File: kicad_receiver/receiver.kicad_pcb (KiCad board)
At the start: 2 copper layers, 60 x 50 mm, 51 parts, among them J1 Conn_01x05_Male, J2 M1+, J3 M1-, J4 M2+, J5 M2-, J6 CHG+5V, J7 CHG-, J8 BAT+, J9 BAT-, U1 LP2985-3.3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

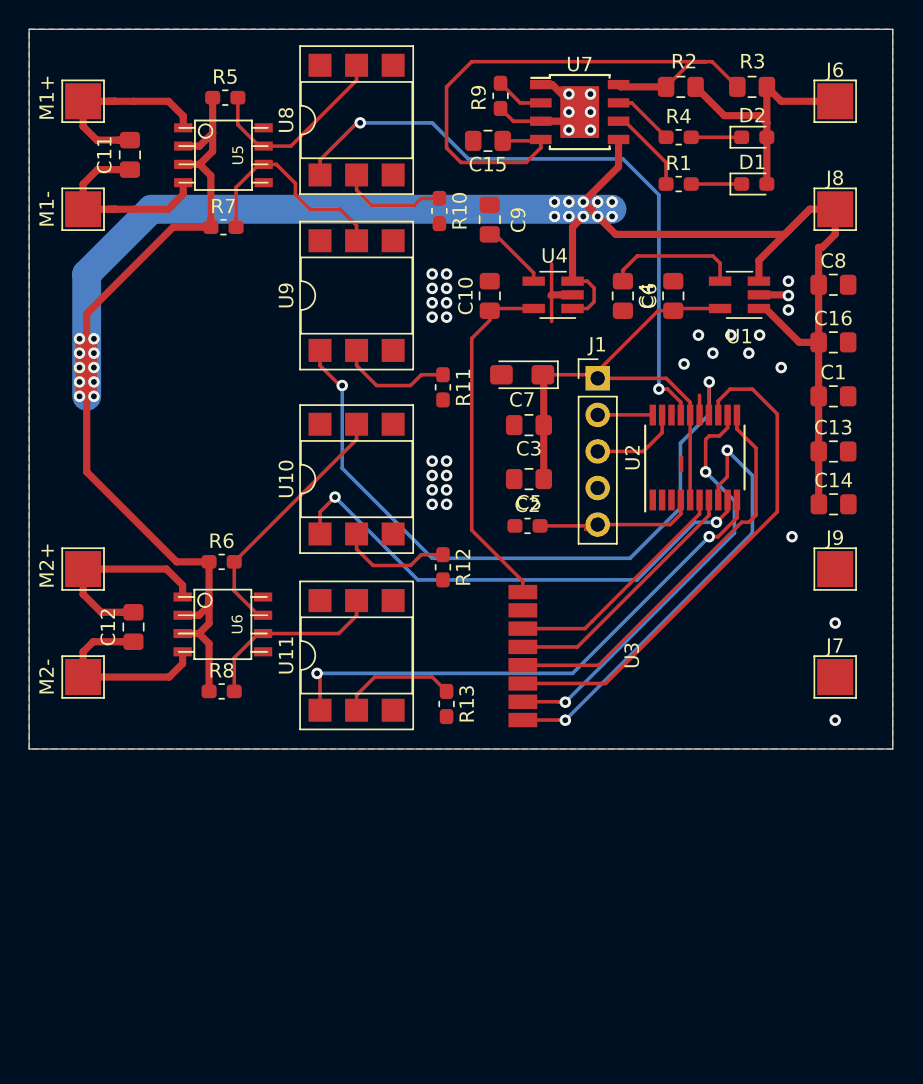
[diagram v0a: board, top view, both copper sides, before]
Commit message: optocouples removed
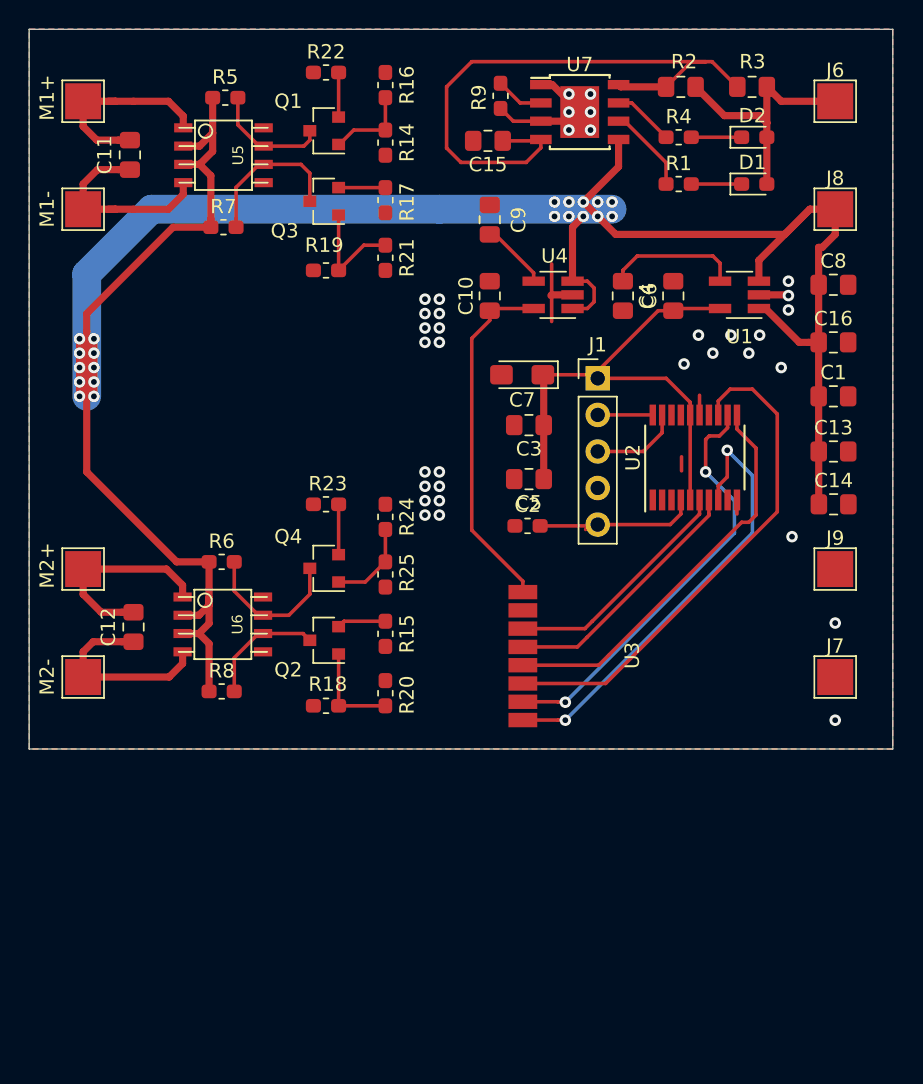
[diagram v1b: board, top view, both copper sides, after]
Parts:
- removed R10, R11, R12, R13: 220, Resistor_SMD:R_0603_1608Metric_Pad1.05x0.95mm_HandSolder
- removed U10, U11, U8, U9: 4N26, Package_DIP:DIP-6_W7.62mm_SMDSocket_SmallPads
- added Q1: MMBT3904, Package_TO_SOT_SMD:SOT-23, F.Cu at (147.5, 82.0)
- added Q2: MMBT3904, Package_TO_SOT_SMD:SOT-23, F.Cu at (147.5, 117.5)
- added Q3: MMBT3904, Package_TO_SOT_SMD:SOT-23, F.Cu at (147.5, 87.0)
- added Q4: MMBT3904, Package_TO_SOT_SMD:SOT-23, F.Cu at (147.5, 112.5)
- added R14: 1k, Resistor_SMD:R_0603_1608Metric_Pad1.05x0.95mm_HandSolder, F.Cu at (151.8, 82.9)
- added R15: 100, Resistor_SMD:R_0603_1608Metric_Pad1.05x0.95mm_HandSolder, F.Cu at (151.8, 117.0)
- added R16: 10k, Resistor_SMD:R_0603_1608Metric_Pad1.05x0.95mm_HandSolder, F.Cu at (151.8, 78.9)
- added R17: 100, Resistor_SMD:R_0603_1608Metric_Pad1.05x0.95mm_HandSolder, F.Cu at (151.8, 86.9)
- added R18: 10k, Resistor_SMD:R_0603_1608Metric_Pad1.05x0.95mm_HandSolder, F.Cu at (147.6, 122.0)
- added R19: 10k, Resistor_SMD:R_0603_1608Metric_Pad1.05x0.95mm_HandSolder, F.Cu at (147.6, 91.8)
- added R20: 1k, Resistor_SMD:R_0603_1608Metric_Pad1.05x0.95mm_HandSolder, F.Cu at (151.8, 121.1)
- added R21: 1k, Resistor_SMD:R_0603_1608Metric_Pad1.05x0.95mm_HandSolder, F.Cu at (151.8, 90.9)
- added R22: 100, Resistor_SMD:R_0603_1608Metric_Pad1.05x0.95mm_HandSolder, F.Cu at (147.6, 78.0)
- added R23: 100, Resistor_SMD:R_0603_1608Metric_Pad1.05x0.95mm_HandSolder, F.Cu at (147.6, 108.0)
- added R24: 10k, Resistor_SMD:R_0603_1608Metric_Pad1.05x0.95mm_HandSolder, F.Cu at (151.8, 108.9)
- added R25: 1k, Resistor_SMD:R_0603_1608Metric_Pad1.05x0.95mm_HandSolder, F.Cu at (151.8, 112.9)
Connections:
- U2 pad 18: Net-(U2-Pad18) -> (no net)
- U2 pad 2: Net-(U2-Pad2) -> (no net)
- U2 pad 3: Net-(U2-Pad3) -> (no net)
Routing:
- net FB_PWM: track 48.3 -> 0.00 mm, vias 2 -> 0
- net FF_PWM: track 44.0 -> 0.00 mm, vias 2 -> 0
- net TURN_RIGHT: track 39.0 -> 1.47 mm, vias 2 -> 0
- net TURN_LEFT: track 35.4 -> 0.00 mm, vias 2 -> 0
- net Net-(R13-Pad1): track 8.24 -> 0.00 mm
- net Net-(R11-Pad1): track 7.94 -> 0.00 mm
- net Net-(R12-Pad1): track 7.83 -> 0.00 mm
- net Net-(Q3-Pad1): track 0.00 -> 7.82 mm
- net Net-(R10-Pad1): track 7.45 -> 0.00 mm
- net Net-(Q4-Pad3): track 17.8 -> 10.4 mm
- net Net-(Q2-Pad1): track 0.00 -> 6.85 mm
- net Net-(Q4-Pad1): track 0.00 -> 6.08 mm
- net Net-(Q1-Pad1): track 0.00 -> 5.91 mm
- net Net-(Q1-Pad3): track 13.7 -> 8.32 mm
- net Net-(Q2-Pad3): track 13.1 -> 8.48 mm
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
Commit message: new route done
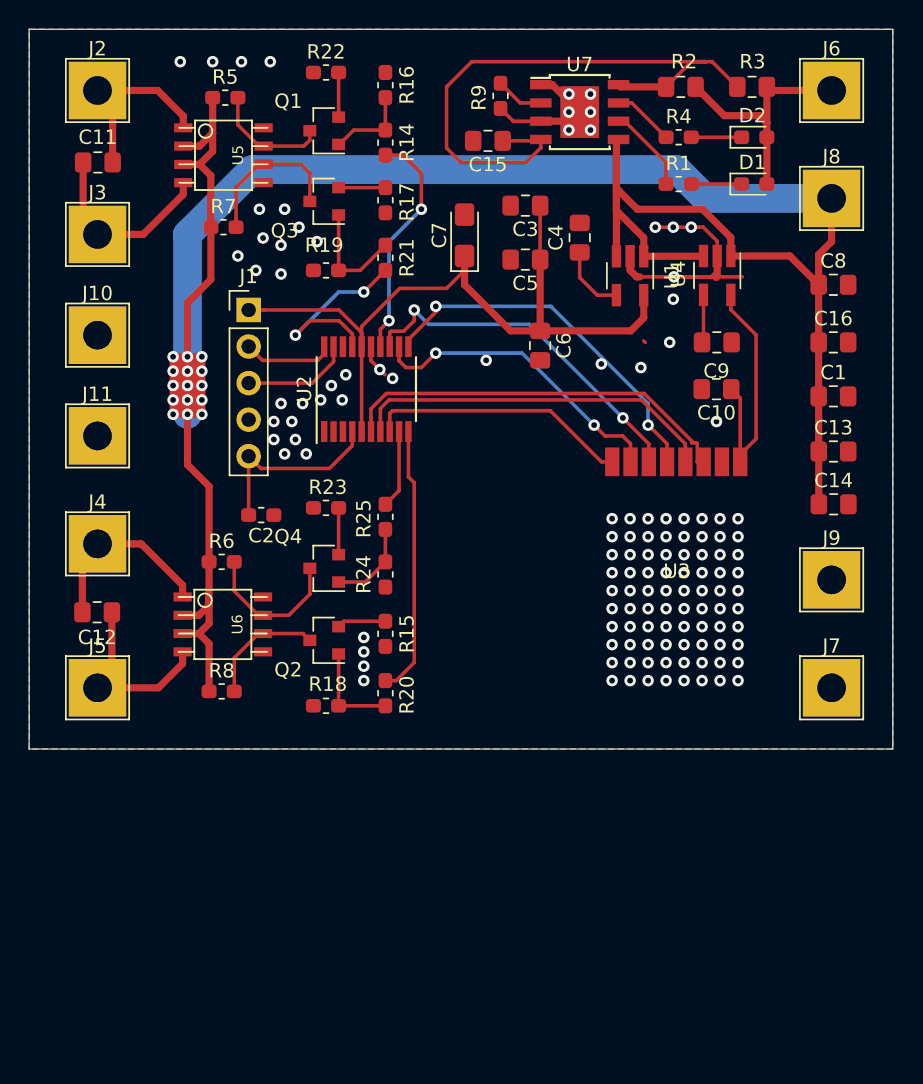
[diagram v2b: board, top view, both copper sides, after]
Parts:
- added J10: LIGHTS, TestPoint:TestPoint_THTPad_4.0x4.0mm_Drill2.0mm, F.Cu at (131.8, 96.2)
- added J11: BEEP, TestPoint:TestPoint_THTPad_4.0x4.0mm_Drill2.0mm, F.Cu at (131.8, 103.2)
- J2, J3, J4, J5, J6, J7, J8, J9: footprint TestPoint:TestPoint_Pad_2.5x2.5mm -> TestPoint:TestPoint_THTPad_4.0x4.0mm_Drill2.0mm
- moved J1 24.7 mm to (142.2, 94.5)
- moved U2 23.3 mm to (150.4, 100.0)
- moved C2 18.5 mm to (143.1, 108.8), turned to 180 degrees
- moved C9 17.9 mm to (174.8, 96.8), turned to 0 degrees
- moved C10 17.0 mm to (174.8, 100.0), turned to 180 degrees
- moved C3 15.3 mm to (161.5, 87.2)
- moved C5 15.3 mm to (161.5, 91.0)
- moved U4 11.5 mm to (174.8, 92.1), turned to 270 degrees
- moved C7 10.5 mm to (157.2, 89.3), turned to 90 degrees
- moved C6 9.87 mm to (162.5, 97.0), turned to 270 degrees
- moved U1 7.72 mm to (168.8, 92.1), turned to 270 degrees
- moved U3 5.15 mm to (172.0, 113.8), turned to 180 degrees
- moved C4 5.04 mm to (165.2, 89.5), turned to 90 degrees
- moved R24 4.00 mm to (151.8, 112.9), turned to 270 degrees
- moved R25 4.00 mm to (151.8, 108.9), turned to 90 degrees
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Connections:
- U2 pad 10: TURN_RIGHT -> TURN_LEFT
- U2 pad 14: FB_PWM -> FF_PWM
- U2 pad 17: FF_PWM -> FB_PWM
- U2 pad 9: TURN_LEFT -> TURN_RIGHT
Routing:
- net TURN_LEFT: track 0.00 -> 18.7 mm
- net FF_PWM: track 0.00 -> 16.7 mm, vias 0 -> 2
- net 3v3mcu: track 36.6 -> 52.0 mm
- net BAT+: track 232.0 -> 217.0 mm, vias 20 -> 15
- net FB_PWM: track 0.00 -> 13.7 mm, vias 0 -> 2
- net NRF_IRQ: track 31.5 -> 18.3 mm, vias 2 -> 0
- net GND: track 19.6 -> 32.6 mm, vias 35 -> 127
- net NRF_CE: track 16.5 -> 27.9 mm
- net SPI_MOSI: track 35.5 -> 25.2 mm, vias 0 -> 2
- net SPI_MISO: track 29.7 -> 21.5 mm
- net NRF_CSN: track 17.8 -> 25.6 mm
- net 3v3radio: track 24.7 -> 18.1 mm
- net Net-(C4-Pad1): track 9.37 -> 4.92 mm
- net TURN_RIGHT: track 1.47 -> 5.44 mm
- net SPI_SCK: track 28.0 -> 25.7 mm, vias 0 -> 2
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
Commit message: mosfets added, piezo scheme added
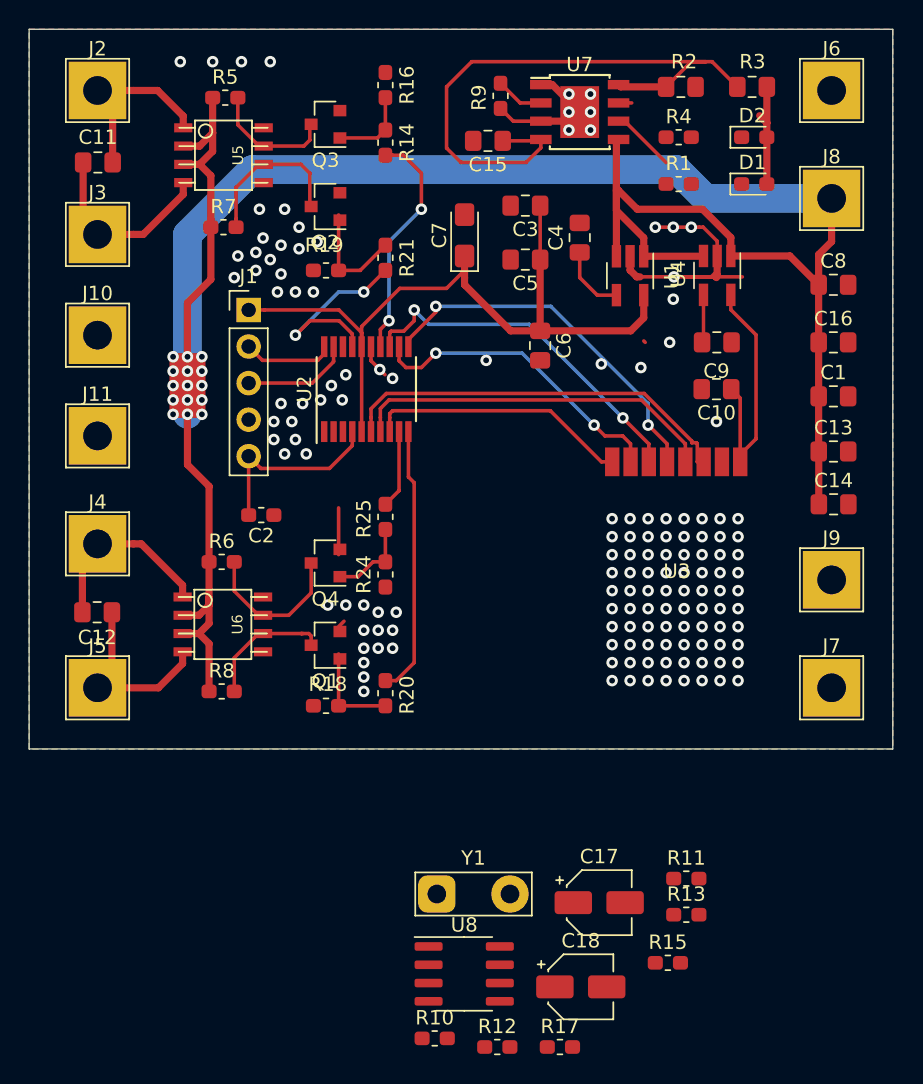
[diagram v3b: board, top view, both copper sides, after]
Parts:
- removed R22, R23: 100, Resistor_SMD:R_0603_1608Metric_Pad1.05x0.95mm_HandSolder
- added C17: 10uf, Capacitor_SMD:CP_Elec_4x3, F.Cu at (166.6, 135.7)
- added C18: 10uf, Capacitor_SMD:CP_Elec_4x3, F.Cu at (165.3, 141.5)
- added R10: 1-10, Resistor_SMD:R_0603_1608Metric_Pad1.05x0.95mm_HandSolder, F.Cu at (155.2, 145.1)
- added R11: 2k2, Resistor_SMD:R_0603_1608Metric_Pad1.05x0.95mm_HandSolder, F.Cu at (172.7, 134.0)
- added R12: 2k2, Resistor_SMD:R_0603_1608Metric_Pad1.05x0.95mm_HandSolder, F.Cu at (159.5, 145.7)
- added R13: 100k, Resistor_SMD:R_0603_1608Metric_Pad1.05x0.95mm_HandSolder, F.Cu at (172.7, 136.5)
- added U8: LM358, Package_SO:SOIC-8_3.9x4.9mm_P1.27mm, F.Cu at (157.2, 140.6)
- added Y1: Crystal, TestPoint:TestPoint_2Pads_Pitch5.08mm_Drill1.3mm, F.Cu at (155.3, 135.1)
- Q1, Q2, Q3, Q4: value MMBT3904 -> BSS138
- R15: value 100 -> 100k
- R17: value 100 -> 1k
- moved R17 60.1 mm to (163.9, 145.7), turned to 0 degrees
- moved Q1 35.7 mm to (147.6, 117.8)
- moved Q2 30.1 mm to (147.6, 87.3)
- moved R15 30.1 mm to (171.4, 139.9), turned to 0 degrees
- moved Q3 5.35 mm to (147.6, 81.6)
- moved Q4 0.38 mm to (147.6, 112.1)
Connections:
- Q1 pad 2: Net-(Q1-Pad2) -> GND
- Q2 pad 2: Net-(Q2-Pad2) -> GND
- Q3 pad 2: Net-(Q3-Pad2) -> GND
- Q4 pad 2: Net-(Q4-Pad2) -> GND
- R14 pad 1: Net-(Q1-Pad1) -> Net-(Q3-Pad1)
- R15 pad 1: GND -> Net-(R15-Pad1)
- R15 pad 2: Net-(Q2-Pad2) -> Net-(R10-Pad1)
- R16 pad 1: Net-(Q1-Pad1) -> Net-(Q3-Pad1)
- R17 pad 1: GND -> (no net)
- R17 pad 2: Net-(Q3-Pad2) -> Net-(R17-Pad2)
- R18 pad 1: Net-(Q2-Pad1) -> Net-(Q1-Pad1)
- R19 pad 1: Net-(Q3-Pad1) -> Net-(Q2-Pad1)
- R20 pad 1: Net-(Q2-Pad1) -> Net-(Q1-Pad1)
- R21 pad 1: Net-(Q3-Pad1) -> Net-(Q2-Pad1)
- R5 pad 2: Net-(Q1-Pad3) -> Net-(Q3-Pad3)
- R7 pad 2: Net-(Q3-Pad3) -> Net-(Q2-Pad3)
- R8 pad 2: Net-(Q2-Pad3) -> Net-(Q1-Pad3)
- U5 pad 6: Net-(Q3-Pad3) -> Net-(Q2-Pad3)
- U5 pad 7: Net-(Q1-Pad3) -> Net-(Q3-Pad3)
- U6 pad 6: Net-(Q2-Pad3) -> Net-(Q1-Pad3)
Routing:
- net Net-(D1-Pad2): track 17.3 -> 7.81 mm
- net GND: track 32.6 -> 36.3 mm, vias 127 -> 144
- net Net-(D2-Pad1): track 3.50 -> 0.00 mm
- net Net-(D1-Pad1): track 3.50 -> 0.00 mm
- net Net-(Q2-Pad2): track 3.41 -> 0.00 mm
- net Net-(R4-Pad1): track 4.29 -> 0.92 mm
- net Net-(Q4-Pad2): track 3.25 -> 0.00 mm
- net Net-(Q3-Pad2): track 3.25 -> 0.00 mm
- net Net-(Q1-Pad2): track 3.10 -> 0.00 mm
- net Net-(Q2-Pad3): track 8.48 -> 10.8 mm
- net Net-(Q3-Pad1): track 7.82 -> 5.64 mm
- net Net-(Q3-Pad3): track 10.8 -> 8.81 mm
- net Net-(R1-Pad1): track 5.98 -> 4.49 mm
- net Net-(Q1-Pad1): track 5.91 -> 7.20 mm
- net Net-(Q2-Pad1): track 6.85 -> 7.82 mm
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
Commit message: piezo route done
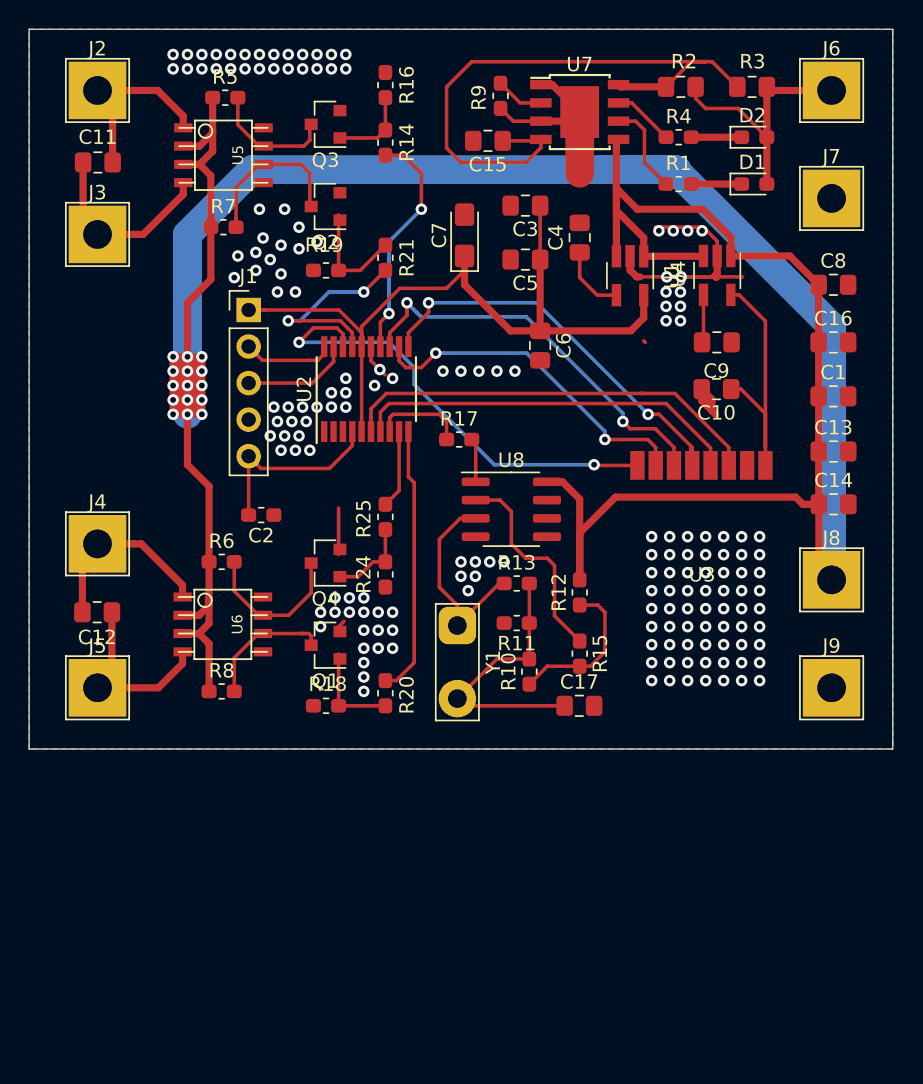
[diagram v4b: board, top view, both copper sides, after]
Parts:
- removed C18: 10uf, Capacitor_SMD:CP_Elec_4x3
- removed J10: LIGHTS, TestPoint:TestPoint_THTPad_4.0x4.0mm_Drill2.0mm
- removed J11: BEEP, TestPoint:TestPoint_THTPad_4.0x4.0mm_Drill2.0mm
- C17: footprint Capacitor_SMD:CP_Elec_4x3 -> Capacitor_SMD:C_0805_2012Metric_Pad1.15x1.40mm_HandSolder
- moved R17 42.8 mm to (156.9, 103.5)
- moved J7 34.0 mm to (182.8, 86.8)
- moved U8 32.4 mm to (160.5, 108.3)
- moved R12 32.1 mm to (165.2, 114.1), turned to 90 degrees
- moved J8 26.5 mm to (182.8, 113.2)
- moved R10 26.3 mm to (161.8, 119.6), turned to 90 degrees
- moved R13 25.9 mm to (160.9, 113.5)
- moved R15 22.3 mm to (165.2, 118.4), turned to 270 degrees
- moved R11 21.3 mm to (160.9, 116.2), turned to 180 degrees
- moved Y1 18.7 mm to (156.8, 116.4), turned to 270 degrees
- moved C17 13.7 mm to (165.2, 122.0)
- moved J9 7.50 mm to (182.8, 120.8)
- moved U3 1.77 mm to (173.8, 114.0)
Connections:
- R17 pad 1: (no net) -> VIBRO_SIGNAL
- U2 pad 18: (no net) -> NRF_IRQ
- U2 pad 8: NRF_IRQ -> VIBRO_SIGNAL
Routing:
- net BAT+: track 217.0 -> 272.3 mm
- net Net-(C17-Pad1): track 0.00 -> 19.3 mm
- net Net-(R15-Pad1): track 0.00 -> 14.6 mm
- net Net-(R13-Pad1): track 0.00 -> 14.1 mm
- net NRF_IRQ: track 18.3 -> 32.2 mm, vias 0 -> 2
- net Net-(R10-Pad1): track 0.00 -> 10.9 mm
- net Net-(D1-Pad2): track 7.81 -> 18.2 mm
- net GND: track 36.3 -> 45.9 mm, vias 144 -> 168
- net VIBRO_SIGNAL: track 0.00 -> 6.48 mm
- net Net-(D2-Pad1): track 0.00 -> 3.50 mm
- net Net-(D1-Pad1): track 0.00 -> 3.50 mm
- net SPI_SCK: track 25.7 -> 29.1 mm
- net Net-(R4-Pad1): track 0.92 -> 4.29 mm
- net SPI_MOSI: track 25.2 -> 28.5 mm
- net Net-(R17-Pad2): track 0.00 -> 3.05 mm
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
